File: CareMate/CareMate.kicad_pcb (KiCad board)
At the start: 2 copper layers, 88.9 x 76.2 mm, 25 parts, among them J1 Barrel_Jack_MountingPin, J2 Conn_01x16, J3 Conn_01x03, J4 Conn_01x03, J5 Conn_01x06, J6 Conn_01x03, J7 Conn_01x03, J8 Conn_01x02, U1 L7805, U2 LM386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

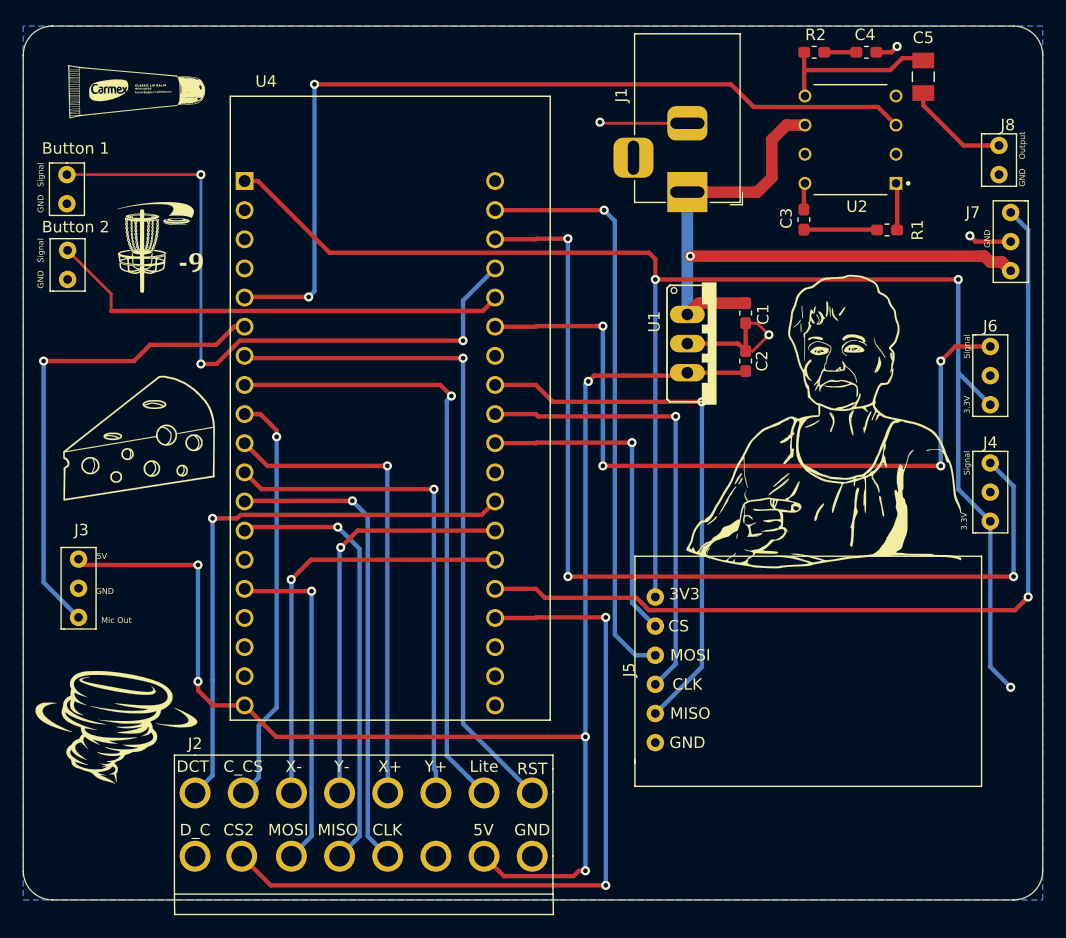
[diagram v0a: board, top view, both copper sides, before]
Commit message: fixed esp gnd
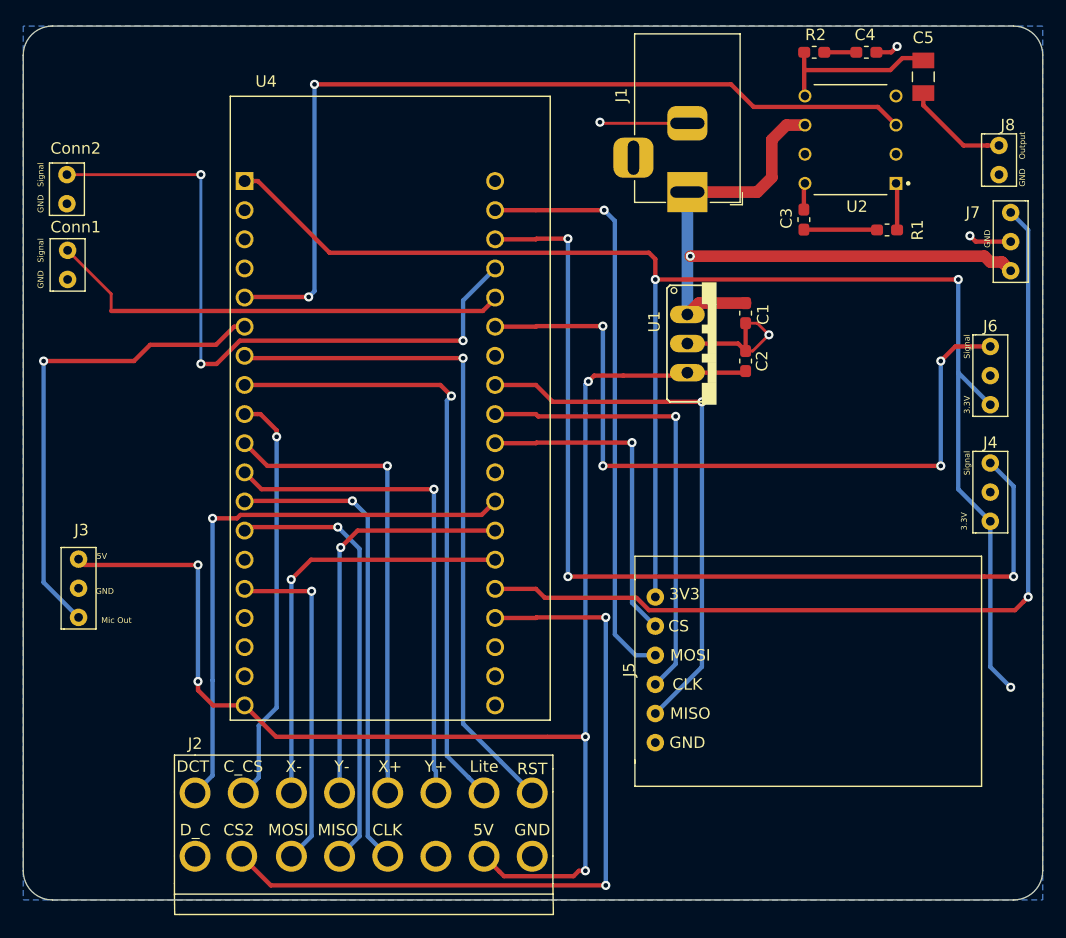
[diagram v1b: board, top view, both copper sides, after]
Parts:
- removed G***: LOGO, Additional Libraries:discgolf
- removed G***: LOGO, Additional Libraries:carmex
- removed G***: LOGO, Additional Libraries:lifealertlady
- removed G***: LOGO, Additional Libraries:cheese
- removed G***: LOGO, Additional Libraries:cyclone
- Conn1: renamed from Button 2
- Conn2: renamed from Button 1
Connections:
- U4 pad 14: Net-(U4-Pad14) -> GND
- U4 pad 20: Net-(U4-Pad20) -> GND
- U4 pad 26: Net-(U4-Pad26) -> GND

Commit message: fixed schematic
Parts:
- removed J6: Conn_01x03, Additional Libraries:Easy_3Pin
- turned U4 to 180 degrees
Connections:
- J2 pad 8: Net-(J2-Pad8) -> D_C
- J2 pad 9: RST -> Net-(J2-Pad9)
- J7 pad 1: +9V -> +5V
- U4 pad 10: X+ -> Servo_1
- U4 pad 11: Y+ -> Mic_Out
- U4 pad 12: clk2 -> clk1
- U4 pad 13: MISO2 -> MISO1
- U4 pad 14: GND -> Net-(U4-Pad14)
- U4 pad 15: MOSI2 -> MOSI1
- U4 pad 21: MOSI1 -> MOSI2
- U4 pad 23: Button_1 -> Net-(U4-Pad23)
- U4 pad 24: Button_2 -> Net-(U4-Pad24)
- U4 pad 25: LS_2 -> D_C
- U4 pad 27: MISO1 -> MISO2
- U4 pad 28: clk1 -> clk2
- U4 pad 29: CS1 -> Card_CS
- U4 pad 30: Net-(U4-Pad30) -> CS2
- U4 pad 32: Y- -> X+
- U4 pad 33: X- -> Y-
- U4 pad 34: Servo_1 -> Lite
- U4 pad 35: CS2 -> CS1
- U4 pad 5: Unamplified_Signal -> Button_1
- U4 pad 6: Mic_Out -> Button_2
- U4 pad 7: RST -> X-
- U4 pad 8: Lite -> Y+
- U4 pad 9: Card_CS -> Unamplified_Signal
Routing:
- net 3.3V: track 135.9 -> 0.00 mm, vias 3 -> 0
- net +5V: track 123.6 -> 0.00 mm, vias 5 -> 0
- net LS_1: track 85.4 -> 0.00 mm, vias 3 -> 0
- net Servo_1: track 82.0 -> 0.00 mm, vias 1 -> 0
- net Unamplified_Signal: track 76.5 -> 0.00 mm, vias 2 -> 0
- net CS2: track 65.8 -> 0.00 mm, vias 2 -> 0
- net LS_2: track 65.1 -> 0.00 mm, vias 4 -> 0
- net RST: track 59.5 -> 0.00 mm, vias 1 -> 0
- net Button_1: track 59.4 -> 0.00 mm, vias 3 -> 0
- net +9V: track 59.2 -> 0.00 mm, vias 1 -> 0
- net Lite: track 54.6 -> 0.00 mm, vias 1 -> 0
- net MOSI1: track 51.2 -> 0.00 mm, vias 1 -> 0
- net Card_Detect: track 49.8 -> 0.00 mm, vias 1 -> 0
- net MISO1: track 47.5 -> 0.00 mm, vias 1 -> 0
- net Y+: track 43.7 -> 0.00 mm, vias 1 -> 0
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
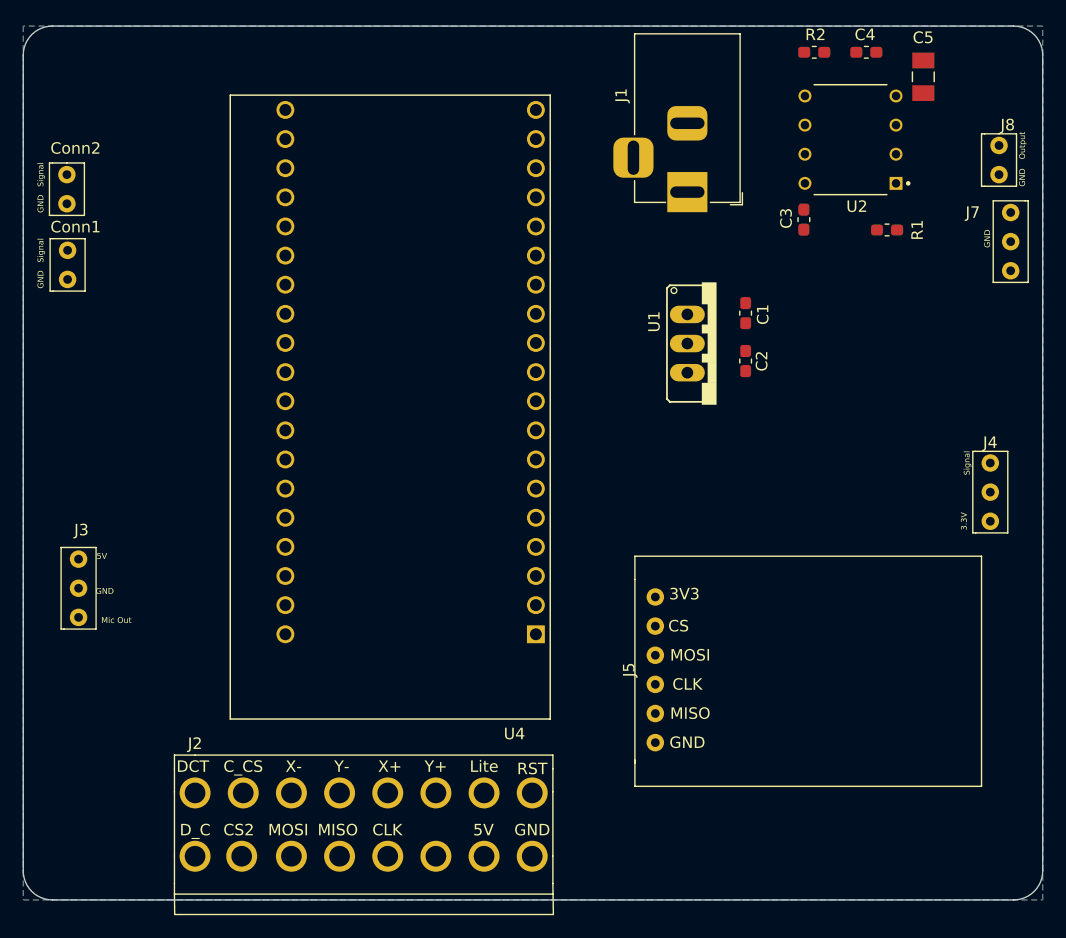
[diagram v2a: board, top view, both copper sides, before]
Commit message: rearranged board layout
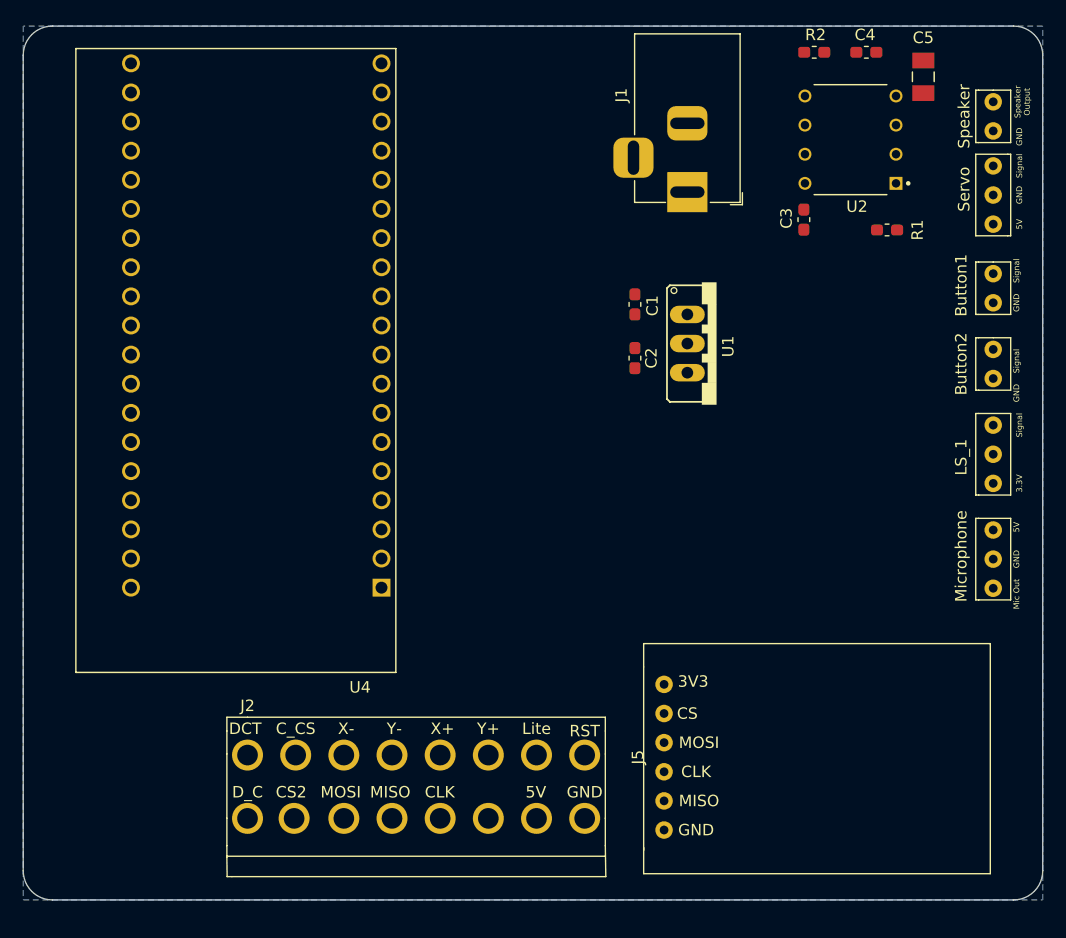
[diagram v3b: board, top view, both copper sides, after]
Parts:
- moved Button1 81.2 mm to (133.6, 44.7)
- moved Button2 81.2 mm to (133.6, 51.3)
- moved Microphone 79.8 mm to (133.1, 67.3)
- moved U4 14.1 mm to (66.8, 54.6)
- moved C1 9.68 mm to (101.6, 49.7)
- moved C2 9.66 mm to (101.6, 54.4)
- moved J5 7.66 mm to (104.1, 89.2)
- moved J2 5.64 mm to (67.8, 86.9)
- moved Servo 4.34 mm to (132.6, 44.7)
- moved Speaker 3.84 mm to (133.6, 29.7)
- moved LS_1 3.31 mm to (133.1, 58.2)
- renumbered Conn2 to Button1, Conn1 to Button2, J4 to LS_1, J3 to Microphone, J7 to Servo, J8 to Speaker
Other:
- board text added: "Speaker Output"
- board text removed: "Output"
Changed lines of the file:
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@@
   (general
     (thickness 1.6)
-    (drawings 22)
+    (drawings 24)
     (tracks 0)
     (zones 0)
@@
   )
   (module ESP32:MODULE_ESP32-DEVKITC-32D (layer F.Cu)
-    (at 80.264 58.674 180)
+    (at 66.802 54.61 180)
     (fp_text reference U4 (at -10.829175 -28.446045) (layer F.SilkS)
       (effects (font (size 1.000386 1.000386) (thickness 0.15)))
@@
   )
   (module "Additional Libraries:16PinConnector" (layer F.Cu)
-    (at 63.246 90.17)
+    (at 67.818 86.868)
     (fp_text reference J2 (at 0 -2.2) (layer F.SilkS)
       (effects (font (size 1 1) (thickness 0.15)))
@@
   )
   (module Capacitor_SMD:C_0603_1608Metric_Pad1.05x0.95mm_HandSolder (layer F.Cu)
-    (at 111.252 50.433 90)
+    (at 101.6 49.671 90)
     (descr "Capacitor SMD 0603 (1608 Metric), square (rectangular) end terminal, IPC_7351 nominal with elongated pad for handsoldering. (Body size source: http://www.tortai-tech.com/upload/download/2011102023233369053.pdf), generated with kicad-footprint-generator")
     (tags "capacitor handsolder")
@@
   )
   (module Capacitor_SMD:C_0603_1608Metric_Pad1.05x0.95mm_HandSolder (layer F.Cu)
-    (at 111.252 54.61 270)
+    (at 101.6 54.356 270)
     (descr "Capacitor SMD 0603 (1608 Metric), square (rectangular) end terminal, IPC_7351 nominal with elongated pad for handsoldering. (Body size source: http://www.tortai-tech.com/upload/download/2011102023233369053.pdf), generated with kicad-footprint-generator")
     (tags "capacitor handsolder")
@@
   )
   (module "Additional Libraries:SD_Card_Reader" (layer F.Cu)
-    (at 103.378 81.534 90)
+    (at 104.14 89.154 90)
     (fp_text reference J5 (at 0 -2.286 90) (layer F.SilkS)
       (effects (font (size 1 1) (thickness 0.15)))
@@
     (at 108.712 53.086 270)
     (descr "<b>VOLTAGE REGULATOR</b>")
-    (fp_text reference U1 (at -1.908575 5.420375 90) (layer F.SilkS)
+    (fp_text reference U1 (at 0.254 -1.016 90) (layer F.SilkS)
       (effects (font (size 1.001882 1.001882) (thickness 0.15)))
     )
@@
   )
   (module "Additional Libraries:Easy_3Pin" (layer F.Cu)
-    (at 53.34 69.85)
-    (fp_text reference J3 (at 0 -0.508) (layer F.SilkS)
+    (at 133.096 67.31)
+    (fp_text reference Microphone (at -3.048 4.318 90) (layer F.SilkS)
       (effects (font (size 1 1) (thickness 0.15)))
     )
@@
   )
   (module "Additional Libraries:Easy_3Pin" (layer F.Cu)
-    (at 132.842 61.468)
-    (fp_text reference J4 (at -0.254 0.254) (layer F.SilkS)
+    (at 133.096 58.166)
+    (fp_text reference LS_1 (at -3.048 4.826 90) (layer F.SilkS)
       (effects (font (size 1 1) (thickness 0.15)))
     )
@@
   )
   (module "Additional Libraries:Easy_3Pin" (layer F.Cu)
-    (at 134.112 48.768 180)
-    (fp_text reference J7 (at 3.048 7.112) (layer F.SilkS)
+    (at 132.588 44.704 180)
+    (fp_text reference Servo (at 2.286 5.08 90) (layer F.SilkS)
       (effects (font (size 1 1) (thickness 0.15)))
     )
@@
   )
   (module "Additional Libraries:Easy_2Pin" (layer F.Cu)
-    (at 134.112 33.528)
-    (fp_text reference J8 (at 0 0.5) (layer F.SilkS)
+    (at 133.604 29.718)
+    (fp_text reference Speaker (at -3.302 3.556 90) (layer F.SilkS)
       (effects (font (size 1 1) (thickness 0.15)))
     )
@@
   )
   (module "Additional Libraries:Easy_2Pin" (layer F.Cu)
-    (at 52.892001 42.668)
-    (fp_text reference Conn1 (at -0.060001 0.258) (layer F.SilkS)
+    (at 133.604 51.308)
+    (fp_text reference Button2 (at -3.556 3.556 90) (layer F.SilkS)
       (effects (font (size 1 1) (thickness 0.15)))
     )
@@
   )
   (module "Additional Libraries:Easy_2Pin" (layer F.Cu)
-    (at 52.832 36.068)
-    (fp_text reference Conn2 (at 0 0) (layer F.SilkS)
+    (at 133.604 44.704)
+    (fp_text reference Button1 (at -3.556 3.302 90) (layer F.SilkS)
       (effects (font (size 1 1) (thickness 0.15)))
     )
@@
       (net 2 GND))
   )
-  (gr_text GND (at 49.784 40.894 90) (layer F.SilkS)
-    (effects (font (size 0.508 0.508) (thickness 0.0762)))
-  )
-  (gr_text GND (at 49.784 47.498 90) (layer F.SilkS)
-    (effects (font (size 0.508 0.508) (thickness 0.0762)))
-  )
-  (gr_text GND (at 55.372 74.676) (layer F.SilkS)
-    (effects (font (size 0.508 0.508) (thickness 0.0762)))
-  )
-  (gr_text GND (at 132.334 43.942 90) (layer F.SilkS)
-    (effects (font (size 0.508 0.508) (thickness 0.0762)))
-  )
-  (gr_text GND (at 135.382 38.608 90) (layer F.SilkS)
-    (effects (font (size 0.508 0.508) (thickness 0.0762)))
-  )
-  (gr_text Output (at 135.382 35.814 90) (layer F.SilkS)
-    (effects (font (size 0.508 0.508) (thickness 0.0762)))
-  )
-  (gr_text Signal (at 130.556 63.5 90) (layer F.SilkS)
-    (effects (font (size 0.508 0.508) (thickness 0.0762)))
-  )
-  (gr_text 3.3V (at 130.302 68.58 90) (layer F.SilkS)
-    (effects (font (size 0.508 0.508) (thickness 0.0762)))
-  )
-  (gr_text 5V (at 55.118 71.628) (layer F.SilkS)
-    (effects (font (size 0.508 0.508) (thickness 0.0762)))
-  )
-  (gr_text "Mic Out" (at 56.388 77.216) (layer F.SilkS)
-    (effects (font (size 0.508 0.508) (thickness 0.0762)))
-  )
-  (gr_text Signal (at 49.784 44.958 90) (layer F.SilkS)
-    (effects (font (size 0.508 0.508) (thickness 0.0762)))
-  )
-  (gr_text Signal (at 49.784 38.354 90) (layer F.SilkS)
-    (effects (font (size 0.508 0.508) (thickness 0.0762)))
-  )
+  (gr_text 5V (at 135.128 42.672 90) (layer F.SilkS)
+    (effects (font (size 0.508 0.508) (thickness 0.0762)))
+  )
+  (gr_text Signal (at 135.128 37.592 90) (layer F.SilkS)
+    (effects (font (size 0.508 0.508) (thickness 0.0762)))
+  )
+  (gr_text GND (at 134.874 71.882 90) (layer F.SilkS)
+    (effects (font (size 0.508 0.508) (thickness 0.0762)))
+  )
+  (gr_text 5V (at 134.874 69.088 90) (layer F.SilkS)
+    (effects (font (size 0.508 0.508) (thickness 0.0762)))
+  )
+  (gr_text "Mic Out" (at 134.874 74.93 90) (layer F.SilkS)
+    (effects (font (size 0.508 0.508) (thickness 0.0762)))
+  )
+  (gr_text GND (at 134.874 49.53 90) (layer F.SilkS)
+    (effects (font (size 0.508 0.508) (thickness 0.0762)))
+  )
+  (gr_text GND (at 134.874 57.404 90) (layer F.SilkS)
+    (effects (font (size 0.508 0.508) (thickness 0.0762)))
+  )
+  (gr_text GND (at 135.128 40.132 90) (layer F.SilkS)
+    (effects (font (size 0.508 0.508) (thickness 0.0762)))
+  )
+  (gr_text GND (at 135.128 35.052 90) (layer F.SilkS)
+    (effects (font (size 0.508 0.508) (thickness 0.0762)))
+  )
+  (gr_text "Speaker\nOutput" (at 135.382 32.004 90) (layer F.SilkS)
+    (effects (font (size 0.508 0.508) (thickness 0.0762)))
+  )
+  (gr_text Signal (at 135.128 60.198 90) (layer F.SilkS)
+    (effects (font (size 0.508 0.508) (thickness 0.0762)))
+  )
+  (gr_text 3.3V (at 135.128 65.278 90) (layer F.SilkS)
+    (effects (font (size 0.508 0.508) (thickness 0.0762)))
+  )
+  (gr_text Signal (at 134.874 54.61 90) (layer F.SilkS)
+    (effects (font (size 0.508 0.508) (thickness 0.0762)))
+  )
+  (gr_text Signal (at 134.874 46.736 90) (layer F.SilkS)
+    (effects (font (size 0.508 0.508) (thickness 0.0762)))
+  )

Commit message: ran traces
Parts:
- moved J5 19.2 mm to (96.8, 71.4)
- moved U4 8.39 mm to (75.2, 54.4)
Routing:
- net +5V: track 0.00 -> 141.3 mm, vias 0 -> 2
- net Lite: track 0.00 -> 85.5 mm, vias 0 -> 2
- net LS_1: track 0.00 -> 74.6 mm, vias 0 -> 2
- net CS1: track 0.00 -> 71.3 mm, vias 0 -> 1
- net Mic_Out: track 0.00 -> 70.0 mm, vias 0 -> 4
- net X+: track 0.00 -> 63.0 mm, vias 0 -> 1
- net Button_1: track 0.00 -> 61.7 mm, vias 0 -> 2
- net Y-: track 0.00 -> 61.7 mm, vias 0 -> 1
- net Unamplified_Signal: track 0.00 -> 61.3 mm, vias 0 -> 1
- net Servo_1: track 0.00 -> 59.3 mm, vias 0 -> 2
- net clk2: track 0.00 -> 57.4 mm, vias 0 -> 1
- net 3.3V: track 0.00 -> 53.4 mm, vias 0 -> 1
- net MISO1: track 0.00 -> 53.1 mm, vias 0 -> 2
- net Button_2: track 0.00 -> 52.9 mm, vias 0 -> 2
- net MISO2: track 0.00 -> 51.2 mm, vias 0 -> 1
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
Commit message: thruholes
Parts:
- added REF**: MountingHole_2.5mm, MountingHole:MountingHole_2.5mm, F.Cu at (53.3, 96.5)
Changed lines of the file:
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@@
     (tracks 212)
     (zones 0)
-    (modules 19)
+    (modules 20)
     (nets 50)
   )
@@
     (add_net clk2)
   )
+  (module MountingHole:MountingHole_2.5mm (layer F.Cu)
+    (at 53.34 96.52)
+    (descr "Mounting Hole 2.5mm, no annular")
+    (tags "mounting hole 2.5mm no annular")
+    (attr virtual)
+    (fp_text reference REF** (at 0 -3.5) (layer F.SilkS)
+      (effects (font (size 1 1) (thickness 0.15)))
+    )
+    (fp_text value MountingHole_2.5mm (at 0 3.5) (layer F.Fab)
+      (effects (font (size 1 1) (thickness 0.15)))
+    )
+    (fp_circle (center 0 0) (end 2.75 0) (layer F.CrtYd) (width 0.05))
+    (fp_circle (center 0 0) (end 2.5 0) (layer Cmts.User) (width 0.15))
+    (fp_text user %R (at 0.3 0) (layer F.Fab)
+      (effects (font (size 1 1) (thickness 0.15)))
+    )
+    (pad 1 np_thru_hole circle (at 0 0) (size 2.5 2.5) (drill 2.5) (layers *.Cu *.Mask))
+  )
   (module ESP32:MODULE_ESP32-DEVKITC-32D (layer F.Cu)
